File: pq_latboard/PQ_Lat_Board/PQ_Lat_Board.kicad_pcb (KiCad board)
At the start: 6 copper layers, 48 x 48 mm, 27 parts, among them IC1 TCN75AVOA713, J1 Conn_01x11_MountingPin, J2 Conn_Coaxial

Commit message: Re-routed the SC, added new SC symbol in schematic, and added pad to solder the comms antenna inside the lateral.
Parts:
- Annotation2: value Snail -> snail
- Annotation3: value pocat_lektron -> pocat-lektron
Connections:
- SC1 pad 2: /SOLAR -> unconnected-(SC1-Pad2)
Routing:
- net /SOLAR: track 38.1 -> 43.5 mm, vias 6 -> 1
- net /PH+: track 34.8 -> 33.1 mm
- net /PH-: track 40.8 -> 39.2 mm
- net GND: vias 9 -> 11
- removed copper zone on F.Cu, net /SOLAR

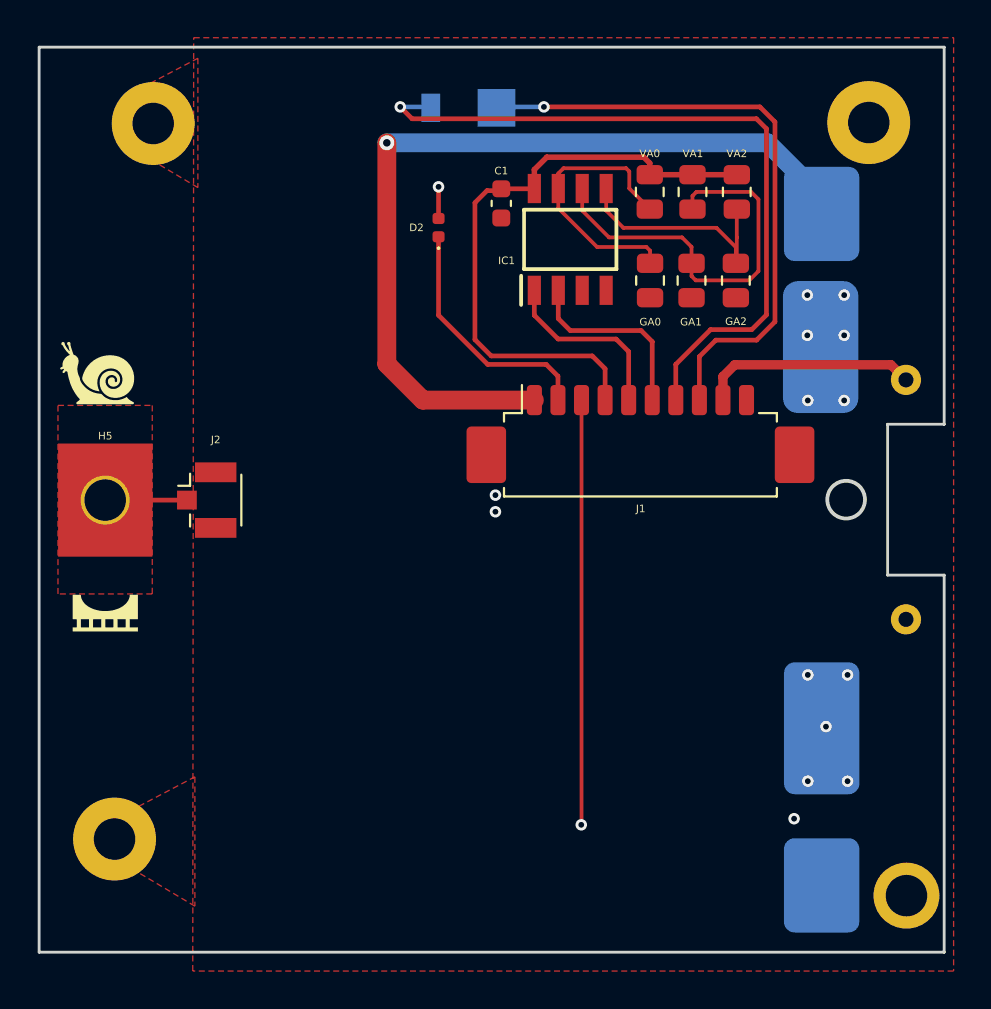
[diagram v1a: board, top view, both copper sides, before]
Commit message: add positive pad behind the Solar Cell to allow soldering the solar cell with epoxy
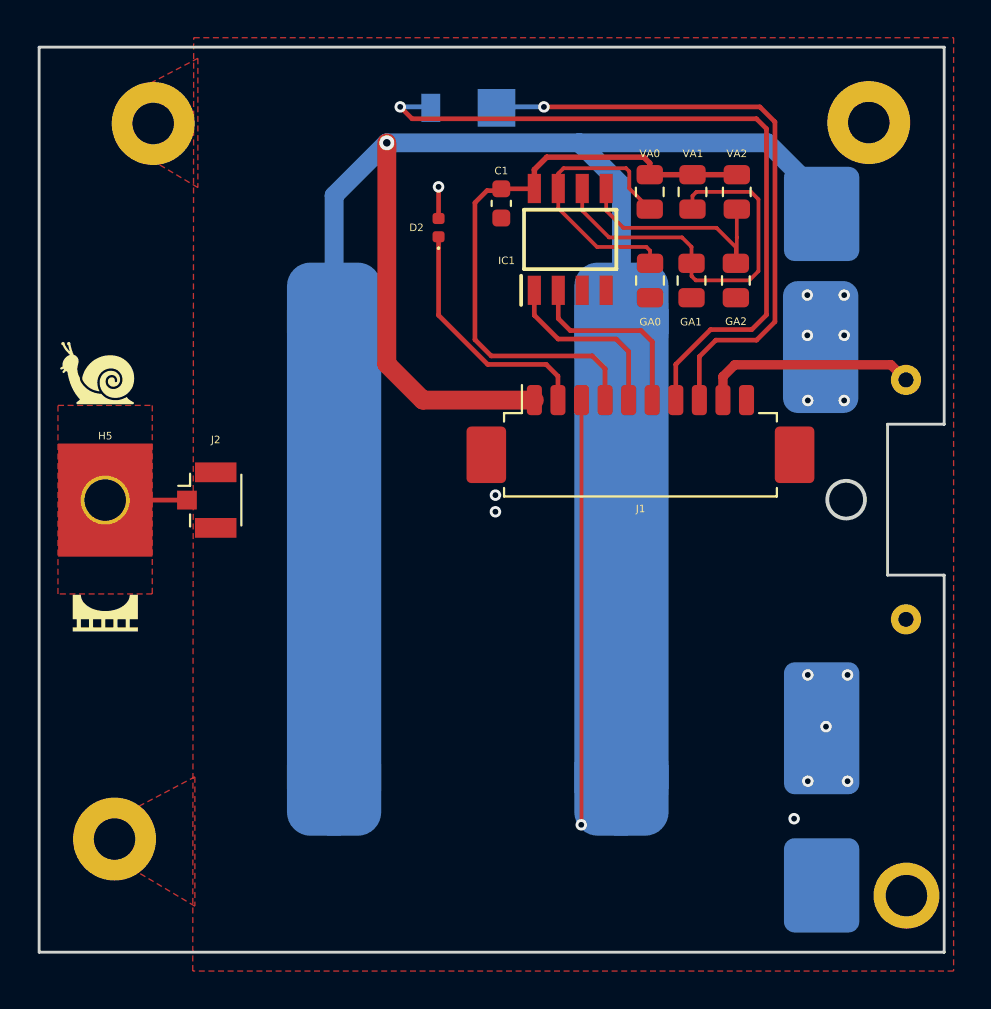
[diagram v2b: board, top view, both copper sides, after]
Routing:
- net /SOLAR: track 43.5 -> 114.1 mm
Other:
- board text added: "+"
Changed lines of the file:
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@@
         (effects (font (size 1 1) (thickness 0.15)) (justify mirror))
     )
-    (fp_text user "-" (at 14.8844 2.286 270 unlocked) (layer "B.SilkS")
+    (fp_text user "-" (at 14.4892 3.5588 unlocked) (layer "B.SilkS")
         (effects (font (size 1 1) (thickness 0.15)) (justify left bottom mirror))
     )
-    (fp_text user "-" (at 25.6032 2.286 270 unlocked) (layer "B.SilkS")
+    (fp_text user "D" (at 6.5644 2.3396 180 unlocked) (layer "B.SilkS")
         (effects (font (size 1 1) (thickness 0.15)) (justify left bottom mirror))
     )
-    (fp_text user "+" (at 5.1816 2.4384 270 unlocked) (layer "B.SilkS")
+    (fp_text user "-" (at 26.224 3.6604 unlocked) (layer "B.SilkS")
         (effects (font (size 1 1) (thickness 0.15)) (justify left bottom mirror))
     )
@@
     (fp_line (start 40.64 0) (end 0 0)
       (stroke (width 0.3) (type default)) (layer "B.SilkS"))
-    (pad "1" smd roundrect (at 10.8204 3 90) (size 7 4) (layers "B.Cu" "B.Paste" "B.Mask") (roundrect_rratio 0.14285725)
+    (pad "1" smd roundrect (at 10.8204 3 90) (size 7 4) (layers "B.Cu" "B.Paste" "B.Mask") (roundrect_rratio 0.1428571429)
       (net 9 "GND") (pintype "passive") (thermal_bridge_angle 45))
     (pad "1" smd roundrect (at 31.0388 2.9464 90) (size 7 4) (layers "B.Cu" "B.Paste" "B.Mask") (roundrect_rratio 0.2)
       (net 9 "GND") (pintype "passive") (thermal_bridge_angle 45))
-    (pad "2" smd roundrect (at 2.4892 2.9972 90) (size 5 4) (layers "B.Cu" "B.Paste" "B.Mask") (roundrect_rratio 0.14285725)
+    (pad "2" smd roundrect (at 2.4892 2.9972 90) (size 5 4) (layers "B.Cu" "B.Paste" "B.Mask") (roundrect_rratio 0.1428571429)
       (net 15 "unconnected-(SC1-Pad2)") (pintype "passive") (thermal_bridge_angle 45))
-    (pad "3" smd roundrect (at 38.1 2.9972 90) (size 5 4) (layers "B.Cu" "B.Paste" "B.Mask") (roundrect_rratio 0.14285725)
+    (pad "3" smd roundrect (at 7.62 -22.86 90) (size 5 5) (layers "B.Cu" "B.Paste" "B.Mask") (roundrect_rratio 0.25)
+      (net 10 "/SOLAR") (pintype "passive") (thermal_bridge_angle 45))
+    (pad "3" smd roundrect (at 7.62 -7.62 90) (size 5 5) (layers "B.Cu" "B.Paste" "B.Mask") (roundrect_rratio 0.25)
+      (net 10 "/SOLAR") (pintype "passive") (thermal_bridge_angle 45))
+    (pad "3" smd roundrect (at 33.02 -22.86 90) (size 5 5) (layers "B.Cu" "B.Paste" "B.Mask") (roundrect_rratio 0.25)
+      (net 10 "/SOLAR") (pintype "passive") (thermal_bridge_angle 45))
+    (pad "3" smd roundrect (at 33.02 -7.62 90) (size 5 5) (layers "B.Cu" "B.Paste" "B.Mask") (roundrect_rratio 0.25)
+      (net 10 "/SOLAR") (pintype "passive") (thermal_bridge_angle 45))
+    (pad "3" smd roundrect (at 38.1 2.9972 90) (size 5 4) (layers "B.Cu" "B.Paste" "B.Mask") (roundrect_rratio 0.1428571429)
       (net 10 "/SOLAR") (pintype "passive") (thermal_bridge_angle 45))
-    (model "${KICAD_NSL_DIR}/power-nsl/StepFiles/Lightricity_S3040_CIC.STEP"
-      (offset (xyz -887.75 -470.5 0.2))
-      (scale (xyz 1 1 1))
-      (rotate (xyz 0 0 0))
-    )
   )
   (footprint "symbols-nsl:Telecos" (layer "B.Cu")
@@
     (effects (font (size 2 2) (thickness 0.3) bold) (justify bottom mirror))
   )
+  (gr_text "+" (at 115.2844 46.9216 180) (layer "B.SilkS")
+    (effects (font (size 1 1) (thickness 0.15)) (justify left bottom mirror))
+  )
   (gr_text "+Y\n" (at 97.11 38.56) (layer "Cmts.User")
     (effects (font (size 5 5) (thickness 0.5)))
@@
   (via (at 93.4404 47.074) (size 0.8) (drill 0.4) (layers "F.Cu" "B.Cu") (net 10))
   (segment (start 113.6334 47.074) (end 115.7162 49.1568) (width 1) (layer "B.Cu") (net 10))
-  (segment (start 93.4404 47.074) (end 113.6334 47.074) (width 1) (layer "B.Cu") (net 10))
+  (segment (start 105.8836 81.3244) (end 105.8836 55.9244) (width 5) (layer "B.Cu") (net 10))
+  (segment (start 93.4404 47.074) (end 103.6512 47.074) (width 1) (layer "B.Cu") (net 10))
+  (segment (start 103.6512 47.074) (end 113.6334 47.074) (width 1) (layer "B.Cu") (net 10))
+  (segment (start 105.8836 49.3064) (end 103.6512 47.074) (width 1) (layer "B.Cu") (net 10))
+  (segment (start 90.6436 49.8708) (end 90.6436 55.9244) (width 1) (layer "B.Cu") (net 10))
+  (segment (start 93.4404 47.074) (end 90.6436 49.8708) (width 1) (layer "B.Cu") (net 10))
+  (segment (start 90.6436 81.3244) (end 90.6436 55.9244) (width 5) (layer "B.Cu") (net 10))
+  (segment (start 105.8836 55.9244) (end 105.8836 49.3064) (width 1) (layer "B.Cu") (net 10))
   (segment (start 96.1836 51.0871) (end 96.1836 49.408) (width 0.25) (layer "F.Cu") (net 11))
   (segment (start 103.7528 83.2436) (end 103.766617 83.229783) (width 0.2) (layer "F.Cu") (net 11))

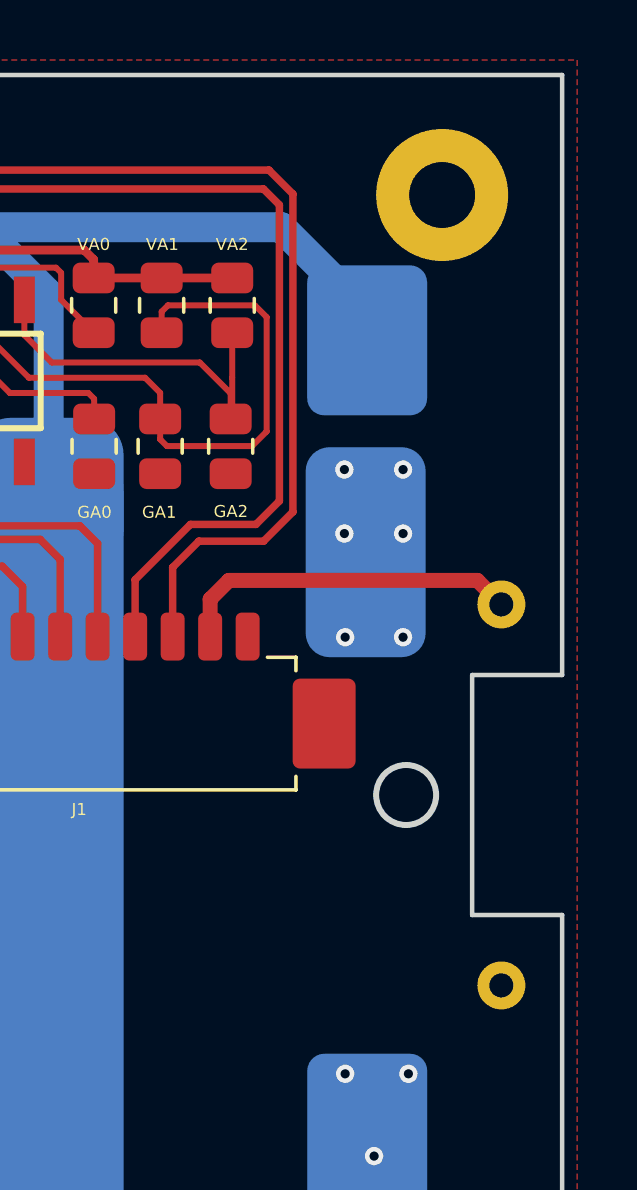
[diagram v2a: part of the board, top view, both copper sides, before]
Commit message: Recenter holes in Lateral PCB as there was a slight misalignment with the top structure
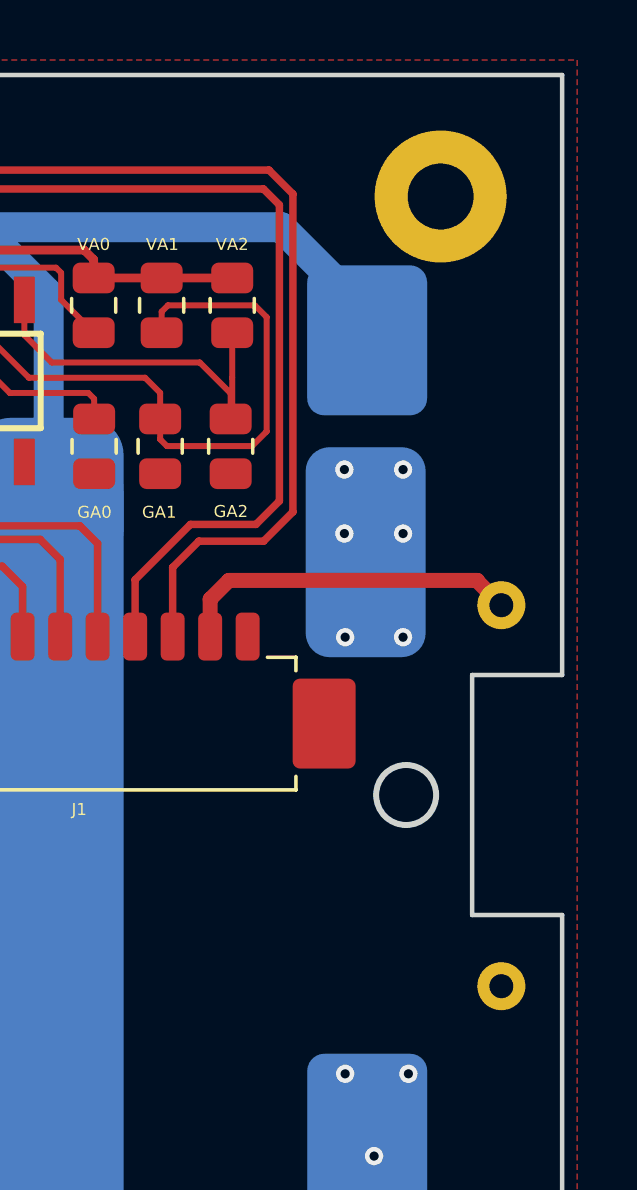
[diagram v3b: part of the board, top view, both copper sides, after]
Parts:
- removed THT1: 7.5, Resistor_THT:R_Axial_DIN0309_L9.0mm_D3.2mm_P12.70mm_Horizontal
- added TK1: 4.7, Resistor_THT:R_Axial_DIN0309_L9.0mm_D3.2mm_P12.70mm_Horizontal, B.Cu at (121.0, 59.7)
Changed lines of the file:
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@@
     (fp_circle (center 0 0) (end 2.45 0)
       (stroke (width 0.05) (type solid)) (fill none) (layer "F.CrtYd"))
-    (pad "1" thru_hole circle (at 0 0) (size 4.4 4.4) (drill 2.2) (layers "*.Cu" "*.Mask")
+    (pad "1" thru_hole circle (at -0.05 0.05) (size 4.4 4.4) (drill 2.2) (layers "*.Cu" "*.Mask")
       (net 9 "GND") (pinfunction "1") (pintype "input") (zone_connect 2))
   )
@@
       (stroke (width 0) (type solid)) (fill solid) (layer "B.SilkS"))
   )
+  (footprint "Resistor_THT:R_Axial_DIN0309_L9.0mm_D3.2mm_P12.70mm_Horizontal" (layer "B.Cu")
+    (at 120.974 59.6724 -90)
+    (descr "Resistor, Axial_DIN0309 series, Axial, Horizontal, pin pitch=12.7mm, 0.5W = 1/2W, length*diameter=9*3.2mm^2, http://cdn-reichelt.de/documents/datenblatt/B400/1_4W%23YAG.pdf")
+    (tags "Resistor Axial_DIN0309 series Axial Horizontal pin pitch 12.7mm 0.5W = 1/2W length 9mm diameter 3.2mm")
+    (property "Manufacturer 1" "Vishay/Dale")
+    (property "Manufacturer Part Number 1" "MRS25000C7508FCT00 ")
+    (property "Sheetfile" "PQ_Lat_Board.kicad_sch")
+    (property "Sheetname" "")
+    (property "Supplier 1" "Mouser")
+    (property "Supplier Part Number 1" "594-MRS25000C7508FCT ")
+    (property "ki_description" "Resistor")
+    (property "ki_keywords" "R res resistor")
+    (attr through_hole)
+    (fp_text reference "TK1" (at 9.144 2.8448 90) (layer "B.SilkS")
+        (effects (font (size 1 1) (thickness 0.15)) (justify mirror))
+    )
+    (fp_text value "4.7" (at 6.35 -2.72 90) (layer "B.Fab")
+        (effects (font (size 1 1) (thickness 0.15)) (justify mirror))
+    )
+    (fp_text user "${REFERENCE}" (at 6.35 0 90) (layer "B.Fab")
+        (effects (font (size 1 1) (thickness 0.15)) (justify mirror))
+    )
+    (fp_line (start 1.04 0) (end 1.73 0)
+      (stroke (width 0.12) (type solid)) (layer "B.SilkS"))
+    (fp_line (start 1.73 -1.72) (end 10.97 -1.72)
+      (stroke (width 0.12) (type solid)) (layer "B.SilkS"))
+    (fp_line (start 1.73 1.72) (end 1.73 -1.72)
+      (stroke (width 0.12) (type solid)) (layer "B.SilkS"))
+    (fp_line (start 10.97 -1.72) (end 10.97 1.72)
+      (stroke (width 0.12) (type solid)) (layer "B.SilkS"))
+    (fp_line (start 10.97 1.72) (end 1.73 1.72)
+      (stroke (width 0.12) (type solid)) (layer "B.SilkS"))
+    (fp_line (start 11.66 0) (end 10.97 0)
+      (stroke (width 0.12) (type solid)) (layer "B.SilkS"))
+    (fp_line (start -1.05 -1.85) (end 13.75 -1.85)
+      (stroke (width 0.05) (type solid)) (layer "B.CrtYd"))
+    (fp_line (start -1.05 1.85) (end -1.05 -1.85)
+      (stroke (width 0.05) (type solid)) (layer "B.CrtYd"))
+    (fp_line (start 13.75 -1.85) (end 13.75 1.85)
+      (stroke (width 0.05) (type solid)) (layer "B.CrtYd"))
+    (fp_line (start 13.75 1.85) (end -1.05 1.85)
+      (stroke (width 0.05) (type solid)) (layer "B.CrtYd"))
+    (fp_line (start 0 0) (end 1.85 0)
+      (stroke (width 0.1) (type solid)) (layer "B.Fab"))
+    (fp_line (start 1.85 -1.6) (end 10.85 -1.6)
+      (stroke (width 0.1) (type solid)) (layer "B.Fab"))
+    (fp_line (start 1.85 1.6) (end 1.85 -1.6)
+      (stroke (width 0.1) (type solid)) (layer "B.Fab"))
+    (fp_line (start 10.85 -1.6) (end 10.85 1.6)
+      (stroke (width 0.1) (type solid)) (layer "B.Fab"))
+    (fp_line (start 10.85 1.6) (end 1.85 1.6)
+      (stroke (width 0.1) (type solid)) (layer "B.Fab"))
+    (fp_line (start 12.7 0) (end 10.85 0)
+      (stroke (width 0.1) (type solid)) (layer "B.Fab"))
+    (pad "1" thru_hole circle (at 0 0 270) (size 1.6 1.6) (drill 0.8) (layers "*.Cu" "*.Mask")
+      (net 5 "/BURNCOMMS") (pintype "passive"))
+    (pad "2" thru_hole oval (at 12.7 0 270) (size 1.6 1.6) (drill 0.8) (layers "*.Cu" "*.Mask")
+      (net 9 "GND") (pintype "passive"))
+    (model "${KICAD6_3DMODEL_DIR}/Resistor_THT.3dshapes/R_Axial_DIN0309_L9.0mm_D3.2mm_P12.70mm_Horizontal.wrl"
+      (offset (xyz 0 0 0))
+      (scale (xyz 1 1 1))
+      (rotate (xyz 0 0 0))
+    )
+  )
   (footprint "passive-nsl:SLCD-61N8" (layer "B.Cu")
     (at 97.6568 45.296 180)
@@
     )
   )
-  (footprint "Resistor_THT:R_Axial_DIN0309_L9.0mm_D3.2mm_P12.70mm_Horizontal" (layer "B.Cu")
-    (at 120.974 59.647 -90)
-    (descr "Resistor, Axial_DIN0309 series, Axial, Horizontal, pin pitch=12.7mm, 0.5W = 1/2W, length*diameter=9*3.2mm^2, http://cdn-reichelt.de/documents/datenblatt/B400/1_4W%23YAG.pdf")
-    (tags "Resistor Axial_DIN0309 series Axial Horizontal pin pitch 12.7mm 0.5W = 1/2W length 9mm diameter 3.2mm")
-    (property "Manufacturer 1" "Vishay/Dale")
-    (property "Manufacturer Part Number 1" "MRS25000C7508FCT00 ")
-    (property "Sheetfile" "PQ_Lat_Board.kicad_sch")
-    (property "Sheetname" "")
-    (property "Supplier 1" "Mouser")
-    (property "Supplier Part Number 1" "594-MRS25000C7508FCT ")
-    (property "ki_description" "Resistor")
-    (property "ki_keywords" "R res resistor")
-    (attr through_hole)
-    (fp_text reference "THT1" (at 6.256 2.1336 90 unlocked) (layer "B.SilkS") hide
-        (effects (font (size 0.4 0.4) (thickness 0.15)) (justify mirror))
-    )
-    (fp_text value "7.5" (at 6.35 -2.72 90) (layer "B.Fab")
-        (effects (font (size 1 1) (thickness 0.15)) (justify mirror))
-    )
-    (fp_text user "${REFERENCE}" (at 6.35 0 90) (layer "B.Fab")
-        (effects (font (size 1 1) (thickness 0.15)) (justify mirror))
-    )
-    (fp_line (start 1.04 0) (end 1.73 0)
-      (stroke (width 0.12) (type solid)) (layer "B.SilkS"))
-    (fp_line (start 1.73 -1.72) (end 10.97 -1.72)
-      (stroke (width 0.12) (type solid)) (layer "B.SilkS"))
-    (fp_line (start 1.73 1.72) (end 1.73 -1.72)
-      (stroke (width 0.12) (type solid)) (layer "B.SilkS"))
-    (fp_line (start 10.97 -1.72) (end 10.97 1.72)
-      (stroke (width 0.12) (type solid)) (layer "B.SilkS"))
-    (fp_line (start 10.97 1.72) (end 1.73 1.72)
-      (stroke (width 0.12) (type solid)) (layer "B.SilkS"))
-    (fp_line (start 11.66 0) (end 10.97 0)
-      (stroke (width 0.12) (type solid)) (layer "B.SilkS"))
-    (fp_line (start -1.05 -1.85) (end 13.75 -1.85)
-      (stroke (width 0.05) (type solid)) (layer "B.CrtYd"))
-    (fp_line (start -1.05 1.85) (end -1.05 -1.85)
-      (stroke (width 0.05) (type solid)) (layer "B.CrtYd"))
-    (fp_line (start 13.75 -1.85) (end 13.75 1.85)
-      (stroke (width 0.05) (type solid)) (layer "B.CrtYd"))
-    (fp_line (start 13.75 1.85) (end -1.05 1.85)
-      (stroke (width 0.05) (type solid)) (layer "B.CrtYd"))
-    (fp_line (start 0 0) (end 1.85 0)
-      (stroke (width 0.1) (type solid)) (layer "B.Fab"))
-    (fp_line (start 1.85 -1.6) (end 10.85 -1.6)
-      (stroke (width 0.1) (type solid)) (layer "B.Fab"))
-    (fp_line (start 1.85 1.6) (end 1.85 -1.6)
-      (stroke (width 0.1) (type solid)) (layer "B.Fab"))
-    (fp_line (start 10.85 -1.6) (end 10.85 1.6)
-      (stroke (width 0.1) (type solid)) (layer "B.Fab"))
-    (fp_line (start 10.85 1.6) (end 1.85 1.6)
-      (stroke (width 0.1) (type solid)) (layer "B.Fab"))
-    (fp_line (start 12.7 0) (end 10.85 0)
-      (stroke (width 0.1) (type solid)) (layer "B.Fab"))
-    (pad "1" thru_hole circle (at 0 0 270) (size 1.6 1.6) (drill 0.8) (layers "*.Cu" "*.Mask")
-      (net 5 "/BURNCOMMS") (pintype "passive"))
-    (pad "2" thru_hole oval (at 12.7 0 270) (size 1.6 1.6) (drill 0.8) (layers "*.Cu" "*.Mask")
-      (net 9 "GND") (pintype "passive"))
-    (model "${KICAD6_3DMODEL_DIR}/Resistor_THT.3dshapes/R_Axial_DIN0309_L9.0mm_D3.2mm_P12.70mm_Horizontal.wrl"
-      (offset (xyz 0 0 0))
-      (scale (xyz 1 1 1))
-      (rotate (xyz 0 0 0))
-    )
-  )
   (gr_line (start 75 90) (end 123 90)
     (stroke (width 0.15) (type solid)) (layer "Edge.Cuts"))
@@
   (segment (start 98.7926 58.827) (end 101.8914 58.827) (width 0.25) (layer "F.Cu") (net 4))
   (segment (start 120.174001 58.847001) (end 111.893399 58.847001) (width 0.5) (layer "F.Cu") (net 5))
+  (segment (start 120.174001 58.847001) (end 120.174001 58.872401) (width 0.5) (layer "F.Cu") (net 5))
   (segment (start 111.893399 58.847001) (end 111.266617 59.473783) (width 0.5) (layer "F.Cu") (net 5))
   (segment (start 111.266617 59.473783) (end 111.266617 60.718784) (width 0.5) (layer "F.Cu") (net 5))
-  (segment (start 120.974 59.647) (end 120.174001 58.847001) (width 0.5) (layer "F.Cu") (net 5))
+  (segment (start 120.174001 58.872401) (end 120.974 59.6724) (width 0.5) (layer "F.Cu") (net 5))
   (segment (start 113.5758 46.3306) (end 113.5758 56.1994) (width 0.25) (layer "F.Cu") (net 6))
   (segment (start 94.1516 45.169) (end 94.7816 45.799) (width 0.25) (layer "F.Cu") (net 6))
